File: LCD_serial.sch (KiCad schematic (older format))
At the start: 5 parts, among them P1 CONN_01X05, U1 74LS164

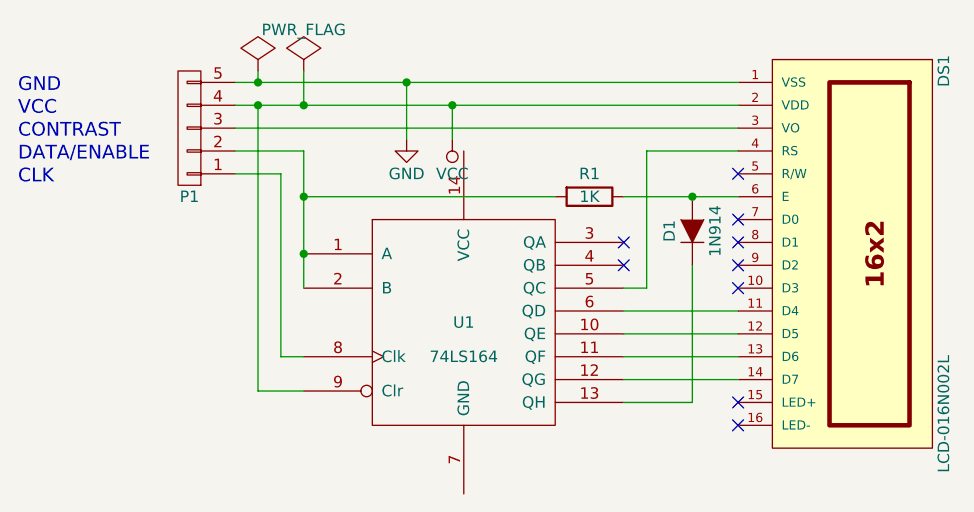
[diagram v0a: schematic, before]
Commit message: Added components Lib and adjusted power connections
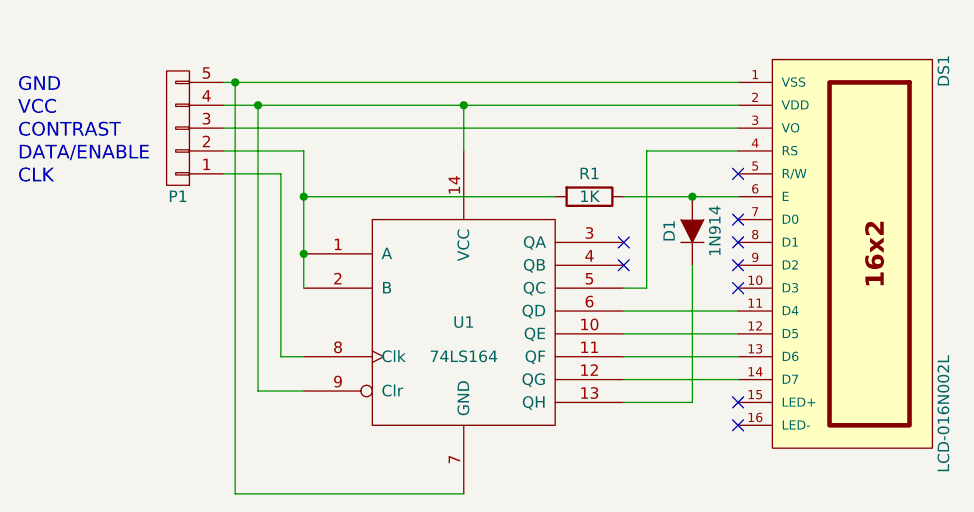
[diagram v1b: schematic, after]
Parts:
- P1: footprint Pin_Headers:Pin_Header_Straight_1x05 -> (none)
- U1: footprint Housings_DIP:DIP-14_W7.62mm_LongPads -> (none)
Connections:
- net GND is gone; now on an unnamed net: DS1.1 (VSS), P1.5 (P5)
- net VCC is gone; now on an unnamed net: DS1.2 (VDD), P1.4 (P4), U1.9 (Clr)
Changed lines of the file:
@@
 LIBS:contrib
 LIBS:valves
-LIBS:74xx_gj
+LIBS:display_lcd
+LIBS:LCD_serial
 LIBS:LCD_serial-cache
 EELAYER 25 0
@@
 Comment4 ""
 $EndDescr
-$Comp
-L 74LS164 U1
-U 1 1 56A7E9D5
-P 5700 3850
-F 0 "U1" H 5700 3850 50  0000 C CNN
-F 1 "74LS164" H 5700 3700 50  0000 C CNN
-F 2 "Housings_DIP:DIP-14_W7.62mm_LongPads" H 5700 3850 50  0001 C CNN
-F 3 "" H 5700 3850 50  0000 C CNN
-	1    5700 3850
-	1    0    0    -1
-$EndComp
 $Comp
 L LCD-016N002L DS1
@@
 	0    -1   -1   0
 $EndComp
-$Comp
-L CONN_01X05 P1
-U 1 1 56A7EBCD
-P 4500 3000
-F 0 "P1" H 4500 3300 50  0000 C CNN
-F 1 "CONN_01X05" V 4600 3000 50  0001 C CNN
-F 2 "Pin_Headers:Pin_Header_Straight_1x05" H 4500 3000 50  0001 C CNN
-F 3 "" H 4500 3000 50  0000 C CNN
-	1    4500 3000
-	-1   0    0    1
-$EndComp
 Wire Wire Line
 	5000 3100 5000 3700
 Wire Wire Line
-	5000 3100 4700 3100
+	5000 3100 4650 3100
 Connection ~ 5000 3550
 Wire Wire Line
@@
 	4900 4000 4900 3200
 Wire Wire Line
-	4900 3200 4700 3200
+	4900 3200 4650 3200
 Wire Wire Line
-	4700 2800 6900 2800
+	4650 2800 6900 2800
 Wire Wire Line
-	4700 2900 6900 2900
+	4650 2900 6900 2900
 Wire Wire Line
-	4700 3000 6900 3000
+	4650 3000 6900 3000
 Wire Wire Line
 	5000 4150 4800 4150
@@
 NoConn ~ 6900 3700
 NoConn ~ 6900 3200
-$Comp
-L PWR_FLAG #FLG01
-U 1 1 56A7EFC6
-P 4800 2750
-F 0 "#FLG01" H 4800 2845 50  0001 C CNN
-F 1 "PWR_FLAG" H 4800 2930 50  0001 C CNN
-F 2 "" H 4800 2750 50  0000 C CNN
-F 3 "" H 4800 2750 50  0000 C CNN
-	1    4800 2750
-	1    0    0    -1
-$EndComp
-$Comp
-L PWR_FLAG #FLG02
-U 1 1 56A7EFE4
-P 5000 2750
-F 0 "#FLG02" H 5000 2845 50  0001 C CNN
-F 1 "PWR_FLAG" H 5000 2930 50  0000 C CNN
-F 2 "" H 5000 2750 50  0000 C CNN
-F 3 "" H 5000 2750 50  0000 C CNN
-	1    5000 2750
-	1    0    0    -1
-$EndComp
-Wire Wire Line
-	5000 2750 5000 2900
-Connection ~ 5000 2900
 Text Notes 3750 2850 0    60   ~ 0
 GND
@@
 Text Notes 3750 3250 0    60   ~ 0
 CLK
-Connection ~ 4800 2800
 Wire Wire Line
-	5450 3050 5450 2800
-Connection ~ 5450 2800
-Wire Wire Line
-	5650 3050 5650 2900
-Connection ~ 5650 2900
+	5700 3100 5700 2900
+Connection ~ 5700 2900
 $Comp
-L GND #PWR03
-U 1 1 56A80727
-P 5450 3050
-F 0 "#PWR03" H 5450 2800 50  0001 C CNN
-F 1 "GND" H 5450 2900 50  0000 C CNN
-F 2 "" H 5450 3050 50  0000 C CNN
-F 3 "" H 5450 3050 50  0000 C CNN
-	1    5450 3050
+L 74LS164 U1
+U 1 1 56A82A63
+P 5700 3850
+F 0 "U1" H 5700 3850 50  0000 C CNN
+F 1 "74LS164" H 5700 3700 50  0000 C CNN
+F 2 "" H 5700 3850 50  0000 C CNN
+F 3 "" H 5700 3850 50  0000 C CNN
+	1    5700 3850
 	1    0    0    -1
 $EndComp
+Wire Wire Line
+	5700 4600 4700 4600
+Wire Wire Line
+	4700 4600 4700 2800
+Connection ~ 4700 2800
 $Comp
-L VCC #PWR04
-U 1 1 56A8075E
-P 5650 3050
-F 0 "#PWR04" H 5650 2900 50  0001 C CNN
-F 1 "VCC" H 5650 3200 50  0000 C CNN
-F 2 "" H 5650 3050 50  0000 C CNN
-F 3 "" H 5650 3050 50  0000 C CNN
-	1    5650 3050
+L CONN_01X05 P1
+U 1 1 56A83287
+P 4450 3000
+F 0 "P1" H 4450 3300 50  0000 C CNN
+F 1 "CONN_01X05" V 4550 3000 50  0001 C CNN
+F 2 "" H 4450 3000 50  0000 C CNN
+F 3 "" H 4450 3000 50  0000 C CNN
+	1    4450 3000
 	-1   0    0    1
 $EndComp
-Wire Wire Line
-	4800 2750 4800 2800
 $EndSCHEMATC

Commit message: Starting on the PCB layout
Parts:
- DS1: footprint Display:LCD-016N002L -> Pin_Headers:Pin_Header_Straight_1x14
- P1: footprint (none) -> Pin_Headers:Pin_Header_Straight_1x05
- U1: footprint (none) -> Housings_DIP:DIP-14_W7.62mm_LongPads
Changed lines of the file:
@@
 F 0 "DS1" H 6600 3950 50  0000 C CNN
 F 1 "LCD-016N002L" H 8100 3950 50  0000 C CNN
-F 2 "Display:LCD-016N002L" H 7400 3500 50  0001 C CIN
+F 2 "Pin_Headers:Pin_Header_Straight_1x14" H 7400 3500 50  0001 C CIN
 F 3 "" H 7400 3550 50  0000 C CNN
 	1    7400 3550
@@
 F 0 "U1" H 5700 3850 50  0000 C CNN
 F 1 "74LS164" H 5700 3700 50  0000 C CNN
-F 2 "" H 5700 3850 50  0000 C CNN
+F 2 "Housings_DIP:DIP-14_W7.62mm_LongPads" H 5700 3850 50  0001 C CNN
 F 3 "" H 5700 3850 50  0000 C CNN
 	1    5700 3850
@@
 $Comp
 L CONN_01X05 P1
-U 1 1 56A83287
+U 1 1 56A87E0E
 P 4450 3000
 F 0 "P1" H 4450 3300 50  0000 C CNN
 F 1 "CONN_01X05" V 4550 3000 50  0001 C CNN
-F 2 "" H 4450 3000 50  0000 C CNN
+F 2 "Pin_Headers:Pin_Header_Straight_1x05" H 4450 3000 50  0001 C CNN
 F 3 "" H 4450 3000 50  0000 C CNN
 	1    4450 3000

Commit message: Rescue library created
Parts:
- P1: symbol CONN_01X05 -> CONN_01X05-RESCUE-LCD_serial
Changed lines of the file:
@@
 EESchema Schematic File Version 2
+LIBS:LCD_serial-rescue
 LIBS:power
 LIBS:device
@@
 Connection ~ 4700 2800
 $Comp
-L CONN_01X05 P1
+L CONN_01X05-RESCUE-LCD_serial P1
 U 1 1 56A87E0E
 P 4450 3000

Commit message: layout progress
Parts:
- removed P1: CONN_01X05, Pin_Headers:Pin_Header_Straight_1x05, symbol CONN_01X05-RESCUE-LCD_serial
- added P1: CONN_01X05_GJ, Pin_Headers:Pin_Header_Straight_1x05, symbol CONN_01X05_GJ
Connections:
- net at DS1.1 (VSS), U1.7 (GND): now also P1.5 (P5)
- net at DS1.2 (VDD), U1.14 (VCC), U1.9 (Clr): now also P1.4 (P4)
- net at DS1.3 (VO): now also P1.3 (P3)
- net at R1.2, U1.1 (A), U1.2 (B): now also P1.2 (P2)
- net at U1.8 (Clk): now also P1.1 (P1)
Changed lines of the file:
@@
 EESchema Schematic File Version 2
-LIBS:LCD_serial-rescue
 LIBS:power
 LIBS:device
@@
 Connection ~ 4700 2800
 $Comp
-L CONN_01X05-RESCUE-LCD_serial P1
-U 1 1 56A87E0E
+L CONN_01X05_GJ P1
+U 1 1 56A96551
 P 4450 3000
 F 0 "P1" H 4450 3300 50  0000 C CNN
-F 1 "CONN_01X05" V 4550 3000 50  0001 C CNN
+F 1 "CONN_01X05_GJ" V 4550 3000 50  0001 C CNN
 F 2 "Pin_Headers:Pin_Header_Straight_1x05" H 4450 3000 50  0001 C CNN
 F 3 "" H 4450 3000 50  0000 C CNN
